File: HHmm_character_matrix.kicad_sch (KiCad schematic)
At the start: 16 parts, among them U22 SN74LVC244A, U23 SM411006N/15, U24 SN74LVC244A, U25 SM411006N/15, U26 SM411006N/15, U27 SM411006N/15

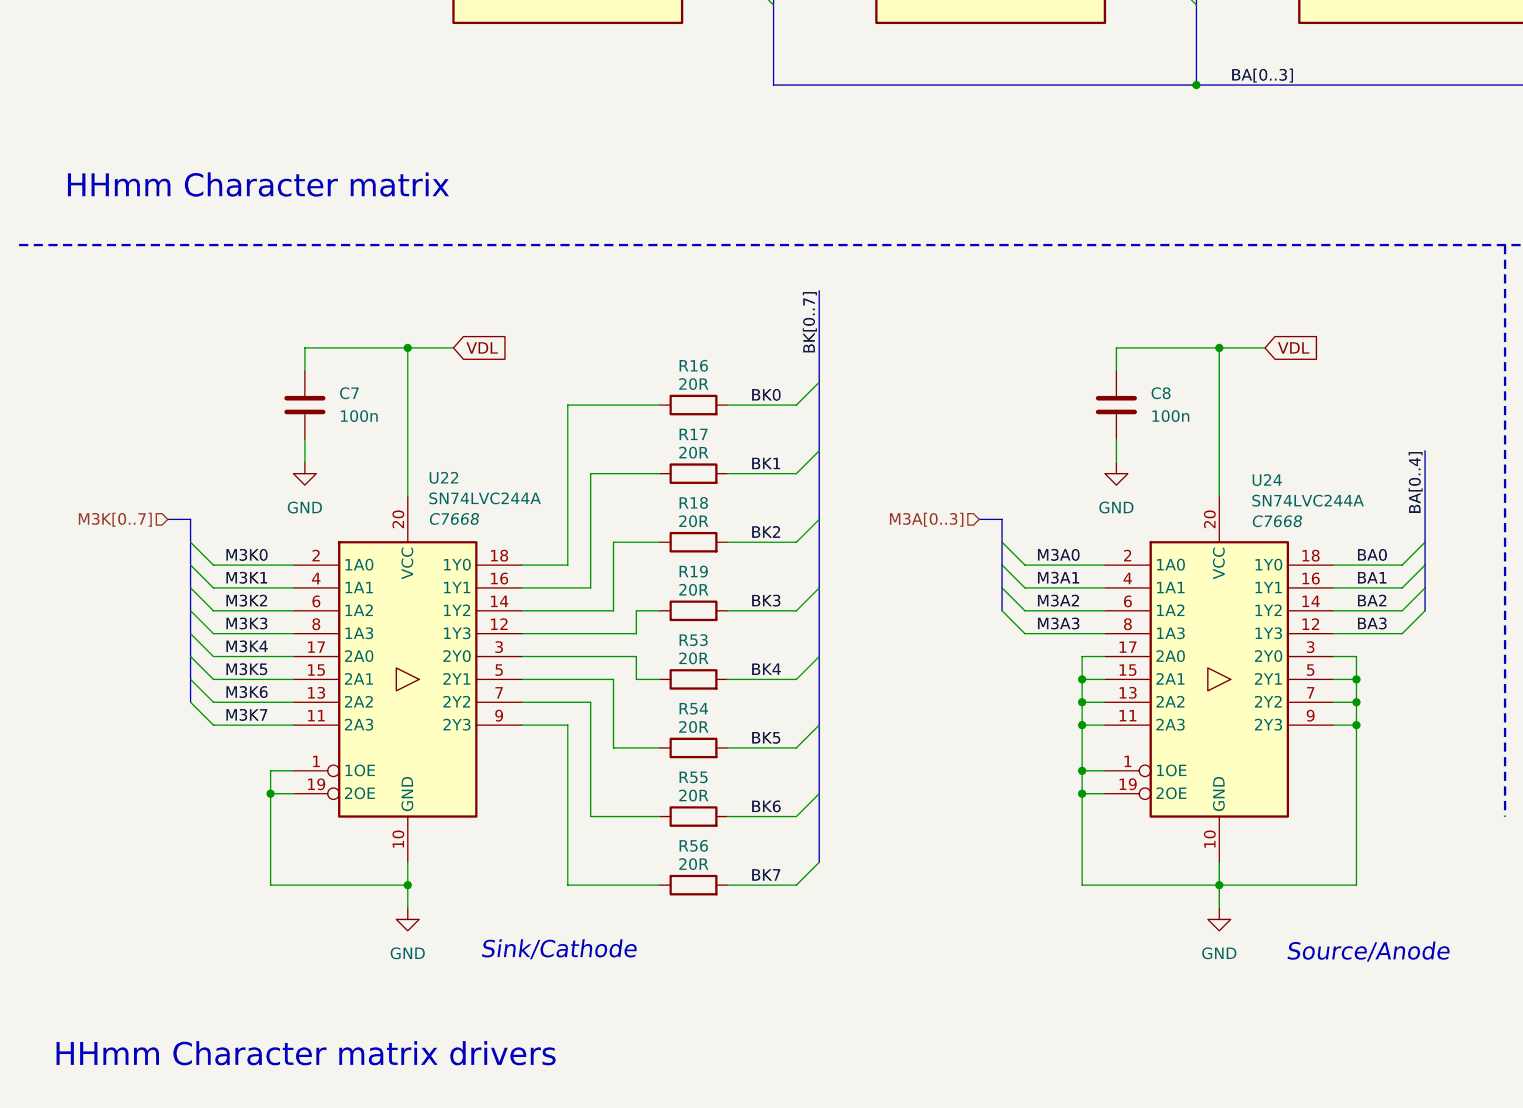
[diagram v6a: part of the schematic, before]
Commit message: verification
- sensor schematic verification
- change in the value of current limiting resistor
- disconnected unused buffer pins
- labeling or peripherals used in primary MCU
- additional user button
- DRC corrections
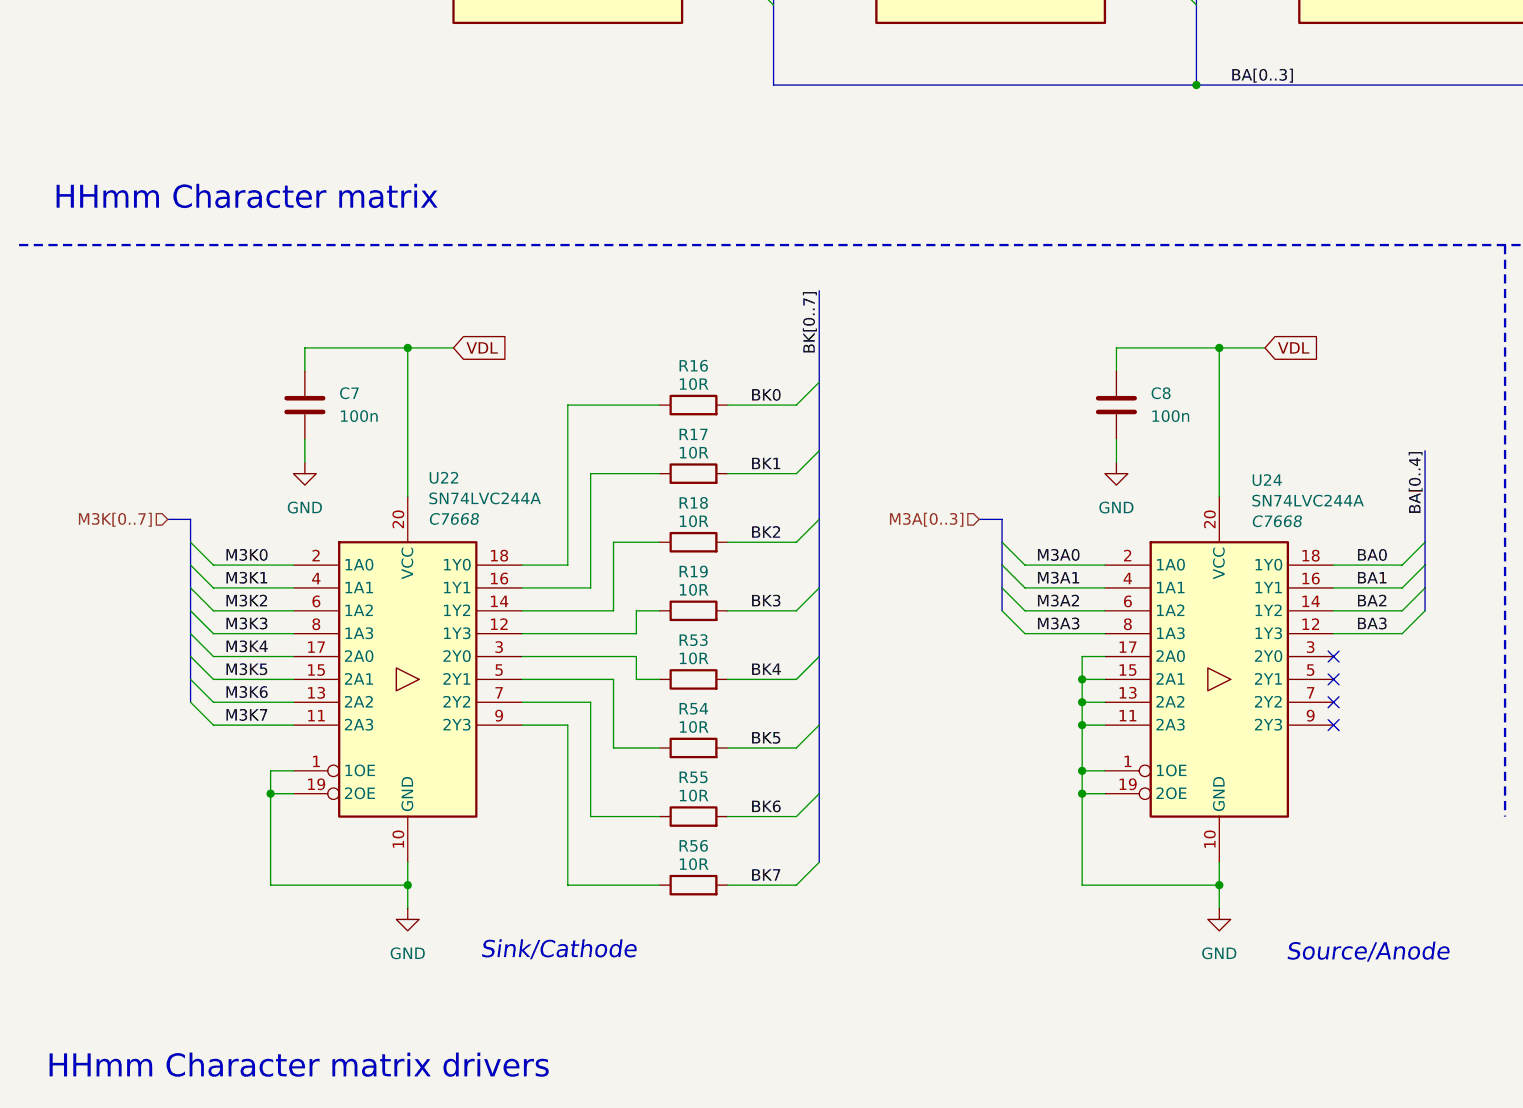
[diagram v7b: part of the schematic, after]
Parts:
- R16, R17, R18, R19, R53, R54, R55, R56: value 20R -> 10R
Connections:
- net GND: no longer U24.3 (2Y0), U24.5 (2Y1), U24.7 (2Y2), U24.9 (2Y3)
- no-connect marks 0 -> 4
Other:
- company: Rajath Katker -> TJ71PL
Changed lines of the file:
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@@
 	(title_block
 		(title "HHmm Character Matrix & Drivers ")
-		(date "2025-11-04")
+		(date "2025-09-05")
 		(rev "v0.0")
-		(company "Rajath Katker")
+		(company "TJ71PL")
+		(comment 1 "天計")
 		(comment 4 "Final verification pending")
 	)
@@
 	(text "HHmm Character matrix drivers "
 		(exclude_from_sim no)
-		(at 16.51 191.77 0)
+		(at 15.748 193.04 0)
 		(effects
 			(font
@@
 	(text "HHmm Character matrix"
 		(exclude_from_sim no)
-		(at 17.78 95.25 0)
+		(at 16.51 96.52 0)
 		(effects
 			(font
@@
 	)
 	(junction
-		(at 161.29 152.4)
-		(diameter 0)
-		(color 0 0 0 0)
-	)
-	(junction
 		(at 55.88 113.03)
 		(diameter 0)
@@
 	)
 	(junction
-		(at 161.29 149.86)
-		(diameter 0)
-		(color 0 0 0 0)
-	)
-	(junction
-		(at 161.29 154.94)
-		(diameter 0)
-		(color 0 0 0 0)
-	)
-	(junction
 		(at 130.81 154.94)
 		(diameter 0)
@@
 		(color 0 0 0 0)
 	)
+	(no_connect
+		(at 158.75 154.94)
+	)
+	(no_connect
+		(at 158.75 147.32)
+	)
+	(no_connect
+		(at 158.75 152.4)
+	)
+	(no_connect
+		(at 158.75 149.86)
+	)
 	(bus_entry
 		(at 144.78 62.23)
@@
 	(wire
 		(pts
-			(xy 158.75 149.86) (xy 161.29 149.86)
-		)
-		(stroke
-			(width 0)
-			(type default)
-		)
-	)
-	(wire
-		(pts
 			(xy 68.58 142.24) (xy 78.74 142.24)
 		)
@@
 	(wire
 		(pts
-			(xy 158.75 147.32) (xy 161.29 147.32)
-		)
-		(stroke
-			(width 0)
-			(type default)
-		)
-	)
-	(wire
-		(pts
 			(xy 55.88 172.72) (xy 55.88 175.26)
 		)
@@
 	(wire
 		(pts
-			(xy 158.75 154.94) (xy 161.29 154.94)
-		)
-		(stroke
-			(width 0)
-			(type default)
-		)
-	)
-	(wire
-		(pts
 			(xy 130.81 149.86) (xy 133.35 149.86)
 		)
@@
 	(wire
 		(pts
-			(xy 161.29 149.86) (xy 161.29 152.4)
-		)
-		(stroke
-			(width 0)
-			(type default)
-		)
-	)
-	(wire
-		(pts
 			(xy 158.75 137.16) (xy 166.37 137.16)
 		)
@@
 	(wire
 		(pts
-			(xy 161.29 154.94) (xy 161.29 172.72)
-		)
-		(stroke
-			(width 0)
-			(type default)
-		)
-	)
-	(wire
-		(pts
 			(xy 91.44 157.48) (xy 99.06 157.48)
 		)
@@
 	(wire
 		(pts
-			(xy 158.75 152.4) (xy 161.29 152.4)
-		)
-		(stroke
-			(width 0)
-			(type default)
-		)
-	)
-	(wire
-		(pts
 			(xy 88.9 69.85) (xy 93.98 69.85)
 		)
@@
 	(wire
 		(pts
-			(xy 161.29 172.72) (xy 146.05 172.72)
-		)
-		(stroke
-			(width 0)
-			(type default)
-		)
-	)
-	(wire
-		(pts
 			(xy 194.31 64.77) (xy 199.39 64.77)
 		)
@@
 	(wire
 		(pts
-			(xy 161.29 152.4) (xy 161.29 154.94)
-		)
-		(stroke
-			(width 0)
-			(type default)
-		)
-	)
-	(wire
-		(pts
 			(xy 147.32 57.15) (xy 152.4 57.15)
 		)
@@
 	(wire
 		(pts
-			(xy 161.29 147.32) (xy 161.29 149.86)
-		)
-		(stroke
-			(width 0)
-			(type default)
-		)
-	)
-	(wire
-		(pts
 			(xy 44.45 123.19) (xy 44.45 125.73)
 		)
@@
 			)
 		)
-		(property "Value" "20R"
+		(property "Value" "10R"
 			(at 87.63 155.194 90)
 			(effects
@@
 			)
 		)
-		(property "Value" "20R"
+		(property "Value" "10R"
 			(at 87.63 162.814 90)
 			(effects
@@
 			)
 		)
-		(property "Value" "20R"
+		(property "Value" "10R"
 			(at 87.63 139.954 90)
 			(effects
@@
 			)
 		)
-		(property "Value" "20R"
+		(property "Value" "10R"
 			(at 87.63 124.714 90)
 			(effects
@@
 			)
 		)
-		(property "Value" "20R"
+		(property "Value" "10R"
 			(at 87.63 170.434 90)
 			(effects
@@
 			)
 		)
-		(property "Value" "20R"
+		(property "Value" "10R"
 			(at 87.63 147.574 90)
 			(effects
@@
 			)
 		)
-		(property "Value" "20R"
+		(property "Value" "10R"
 			(at 87.63 117.094 90)
 			(effects
@@
 			)
 		)
-		(property "Value" "20R"
+		(property "Value" "10R"
 			(at 87.63 132.334 90)
 			(effects

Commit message: semi final verification
- change in display type to common cathode
- verification of the schematic
- addition of footprints
- further minor changes
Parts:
- removed U23, U25, U26, U27: SM411006N/15, precision_clock:SM411006N15, symbol precision_clock:SM411006N/15
- added U23, U25, U26, U27: 10016AS, precision_clock:10016AS, symbol precision_clock:10016AS
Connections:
- net BA0: now also R16.2, U23.7 (A), U25.7 (A), U26.7 (A); no longer U24.18 (1Y0)
- net BA1: now also R17.2, U23.6 (B), U25.6 (B), U26.6 (B), U27.6 (B), U27.7 (A); no longer U24.16 (1Y1)
- net BA2: now also R18.2, U23.4 (C), U25.4 (C), U26.4 (C), U27.4 (C); no longer U24.14 (1Y2)
- net BA3: now also R19.2, U23.2 (D), U25.2 (D), U26.2 (D), U27.2 (D); no longer U24.12 (1Y3)
- net BK0: now also U24.18 (1Y0), U23.3 (CK), U23.8 (CK); no longer R16.2
- net BK1: now also U24.16 (1Y1), U25.3 (CK), U25.8 (CK); no longer R17.2
- net BK2: now also U24.14 (1Y2), U26.3 (CK), U26.8 (CK); no longer R18.2
- net BK3: now also U24.12 (1Y3), U27.3 (CK), U27.8 (CK); no longer R19.2
- net M3A0: now also U22.2 (1A0); no longer U24.2 (1A0)
- net M3A1: now also U22.4 (1A1); no longer U24.4 (1A1)
- net M3A2: now also U22.6 (1A2); no longer U24.6 (1A2)
- net M3A3: now also U22.8 (1A3); no longer U24.8 (1A3)
- net M3K0: now also U24.2 (1A0); no longer U22.2 (1A0)
- net M3K1: now also U24.4 (1A1); no longer U22.4 (1A1)
- net M3K2: now also U24.6 (1A2); no longer U22.6 (1A2)
- net M3K3: now also U24.8 (1A3); no longer U22.8 (1A3)
- net BK4 renamed BA4
- net BA4: now also U23.1 (E), U25.1 (E), U26.1 (E), U27.1 (E)
- net BK5 renamed BA5
- net BA5: now also U23.9 (F), U25.9 (F), U26.9 (F), U27.9 (F)
- net BK6 renamed BA6
- net BA6: now also U23.10 (G), U25.10 (G), U26.10 (G), U27.10 (G)
- net BK7 renamed BA7
- net BA7: now also U23.5 (DP), U25.5 (DP), U26.5 (DP), U27.5 (DP)
- net M3K4 renamed M3A4
- net M3K5 renamed M3A5
- net M3K6 renamed M3A6
- net M3K7 renamed M3A7
